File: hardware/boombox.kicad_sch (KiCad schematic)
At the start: 34 parts, among them J1 Micro_SD_Card_Det1, J4 USB_C_Receptacle_USB2.0_16P, J5 AudioJack4, SW1 SW_SPST, SW2 SW_SPST, SW3 SW_SPST, SW4 SW_SPST, SW5 SW_SPST, U1 Pico, U10 MAX98365A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

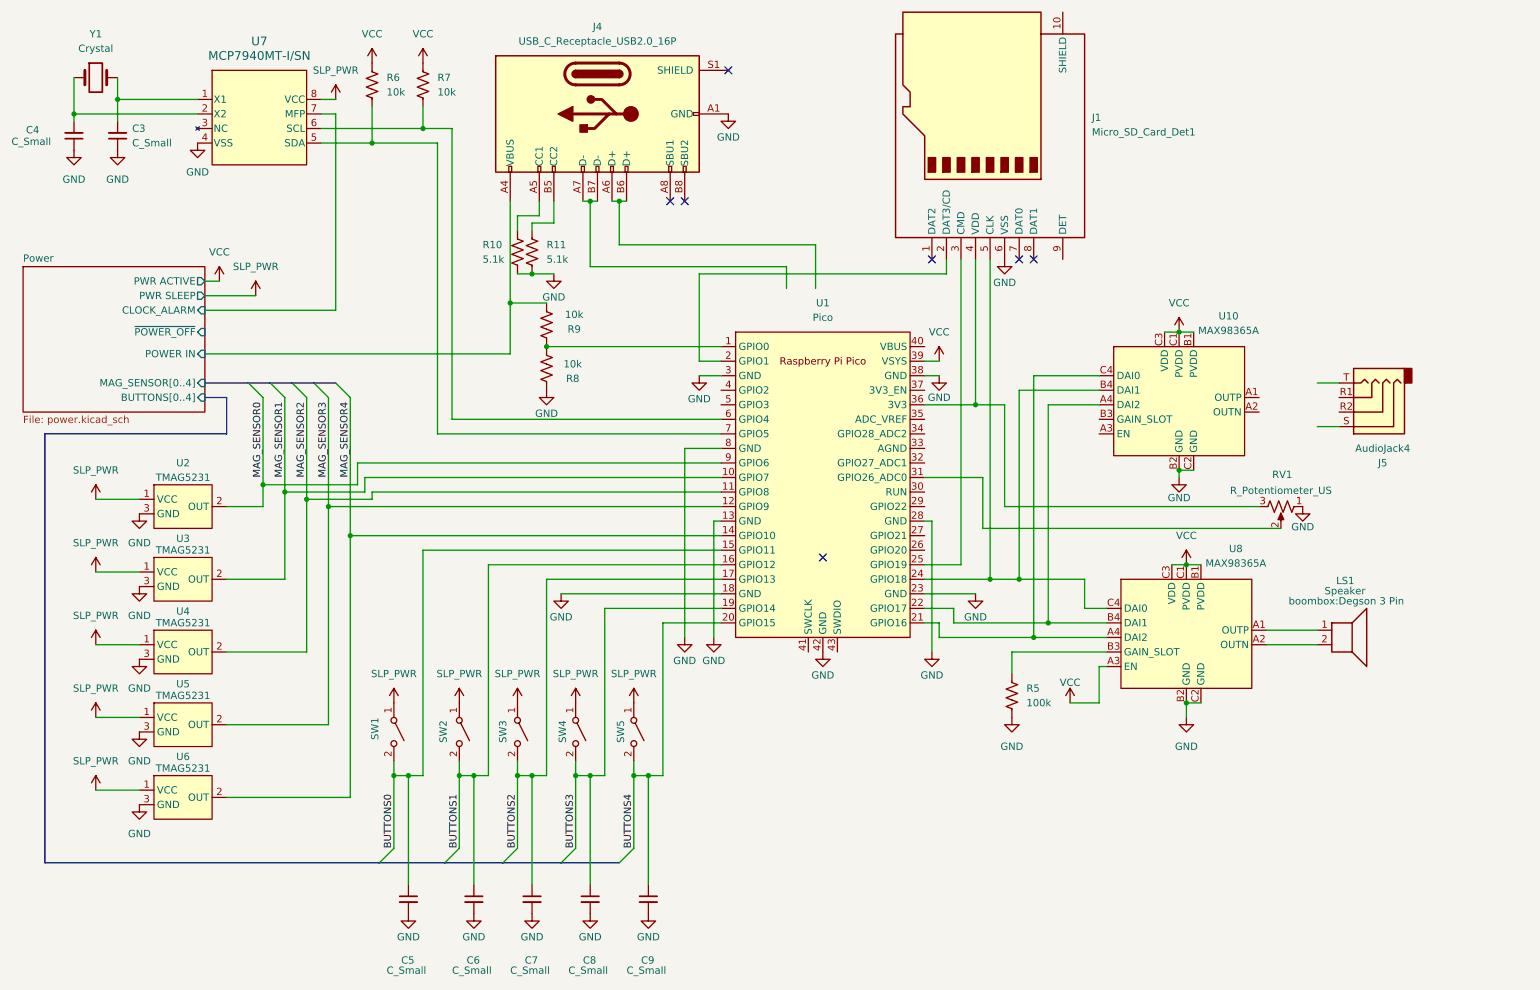
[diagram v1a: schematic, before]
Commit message: Schematic done
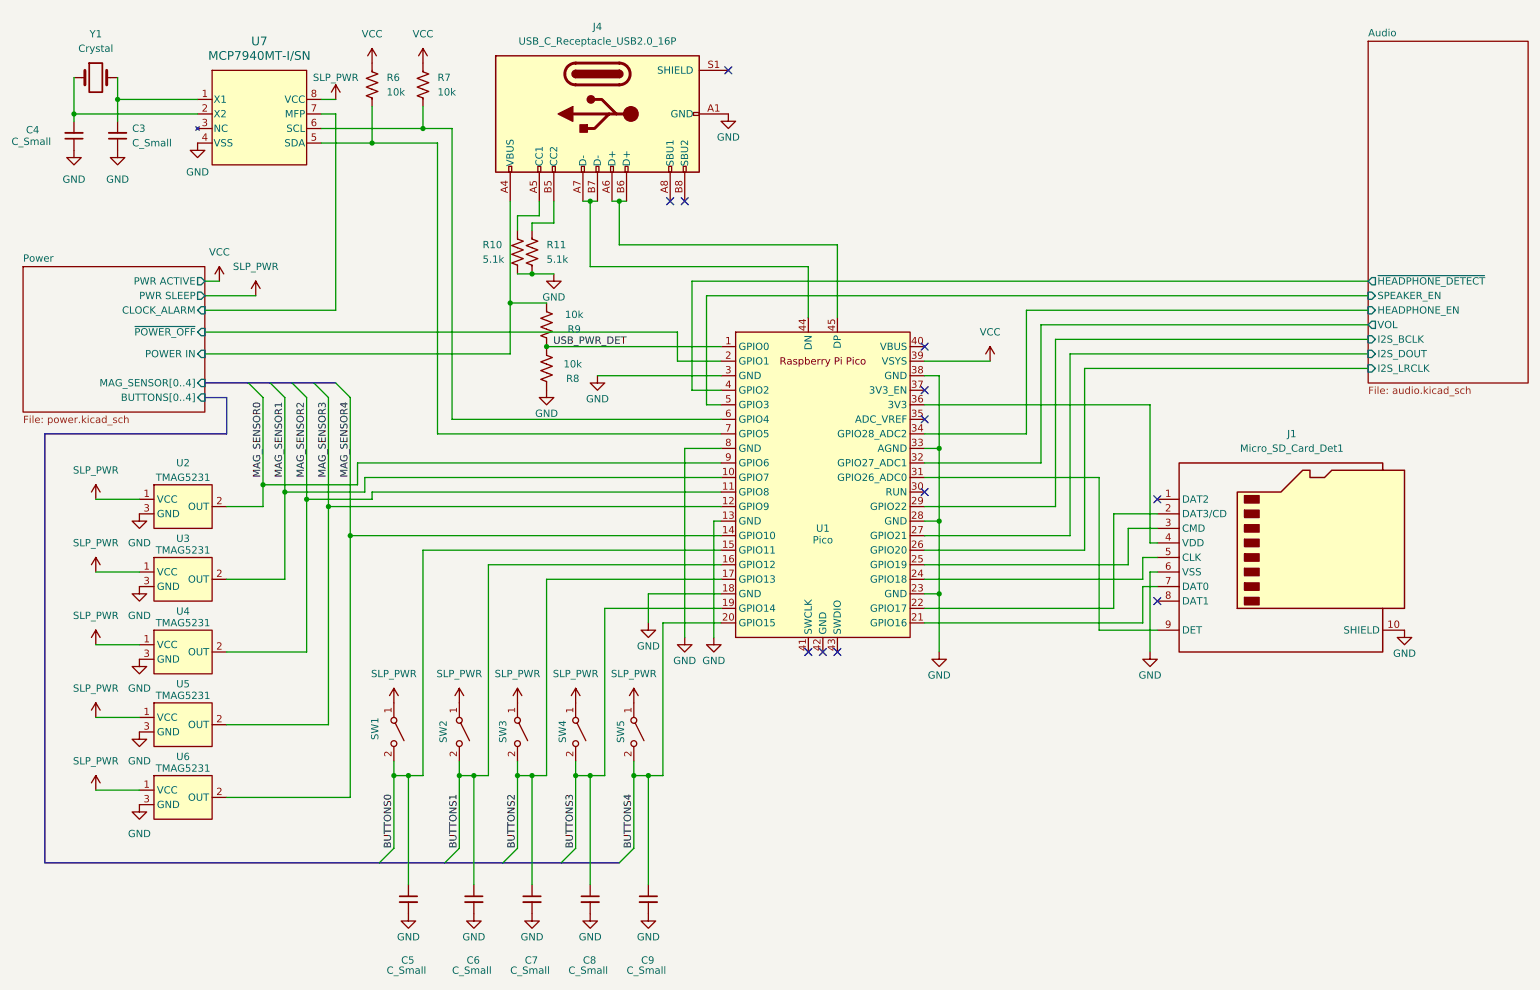
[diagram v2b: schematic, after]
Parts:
- removed J5: AudioJack4, boombox:Degson 3 Pin, symbol Connector_Audio:AudioJack4
- removed LS1: Speaker, boombox:Degson 3 Pin, symbol Device:Speaker
- removed R5: 100k, symbol Device:R_US
- removed RV1: R_Potentiometer_US, boombox:Degson 3 Pin, symbol Device:R_Potentiometer_US
- removed U10, U8: MAX98365A, symbol boombox:MAX98365A
- R10, R11, R6, R7, R8, R9: footprint (none) -> Resistor_SMD:R_0402_1005Metric_Pad0.72x0.64mm_HandSolder
- SW1, SW2, SW3, SW4, SW5: footprint (none) -> boombox:PTS645S_SMTR92_CNK
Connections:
- net GND: now also J1.10 (SHIELD), U1.33 (AGND); no longer U1.42 (GND)
- net Power/~{POWER_OFF}: now also U1.2 (GPIO1)
- net USB_PWR_DET: now reaches R8.2, R9.1, U1.1 (GPIO0)
- net at U1.21 (GPIO16): now also J1.7 (DAT0)
- net at U1.22 (GPIO17): now also J1.2 (DAT3/CD)
- net at U1.31 (GPIO26_ADC0): now also J1.9 (DET)
- net Audio/I2S_LRCLK: now reaches U1.26 (GPIO20)
- net Audio/I2S_DOUT: now reaches U1.27 (GPIO21)
- net Audio/I2S_BCLK: now reaches U1.29 (GPIO22)
- net Audio/VOL: now reaches U1.32 (GPIO27_ADC1)
- net Audio/HEADPHONE_EN: now reaches U1.34 (GPIO28_ADC2)
- net Audio/~{HEADPHONE_DETECT}: now reaches U1.4 (GPIO2)
- net Audio/SPEAKER_EN: now reaches U1.5 (GPIO3)
- net at J4.A6 (D+), J4.B6 (D+): now also U1.45 (DP)
- net at J4.A7 (D-), J4.B7 (D-): now also U1.44 (DN)
- no-connect marks 7 -> 12
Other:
- added sheet Audio (audio.kicad_sch)
- moved on the sheet: J1
